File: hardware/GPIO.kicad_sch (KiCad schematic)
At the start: 21 parts, among them J10 USB_B, J8 Conn_02x10_Odd_Even, J9 Conn_01x06_Male, SW1 SW_Push, U1 MCP23008-xP, U3 PIC18F4550-IP, U4 74LS06, U5 74LS06

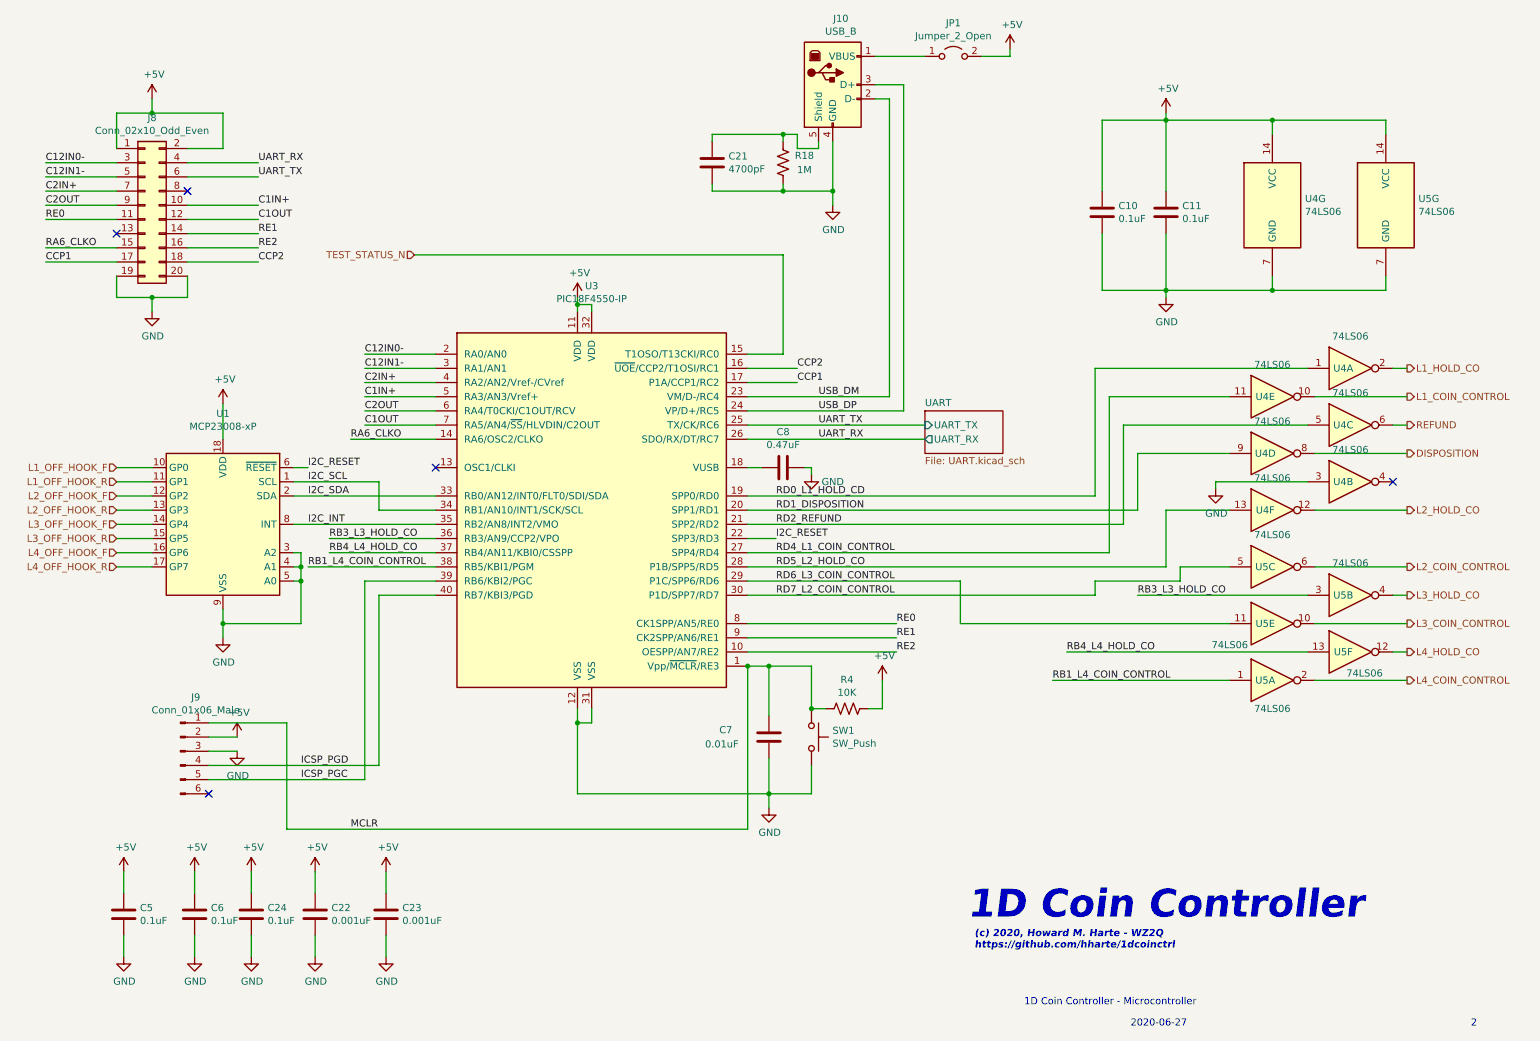
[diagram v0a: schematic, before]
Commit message: Issue 3:
* Remove barrel jack, replace with 4-position terminal block with
  provision for +/- 130VDC input in case the user already has an
  appropriate power supply and does not want the on-board
  DC-DC converter.  Note: 130V DC-DC converter PS2, relay
  K8, C14, D10, and R16 must be omitted during assembly.
* Add bi-color LEDs for line status.
  Green=Off-hook, normal polarity.
  Red=Off-hook, reverse polarity.
  Off=on-hook.
* Add header for FTDI USB UART, if user does not RS-232 UART levels.
  To use the FTDI header, do not populate U1 and other components on
  pp. 3 of the schematic.
* Remove i2c I/O expander and use PIC GPIOs directly.
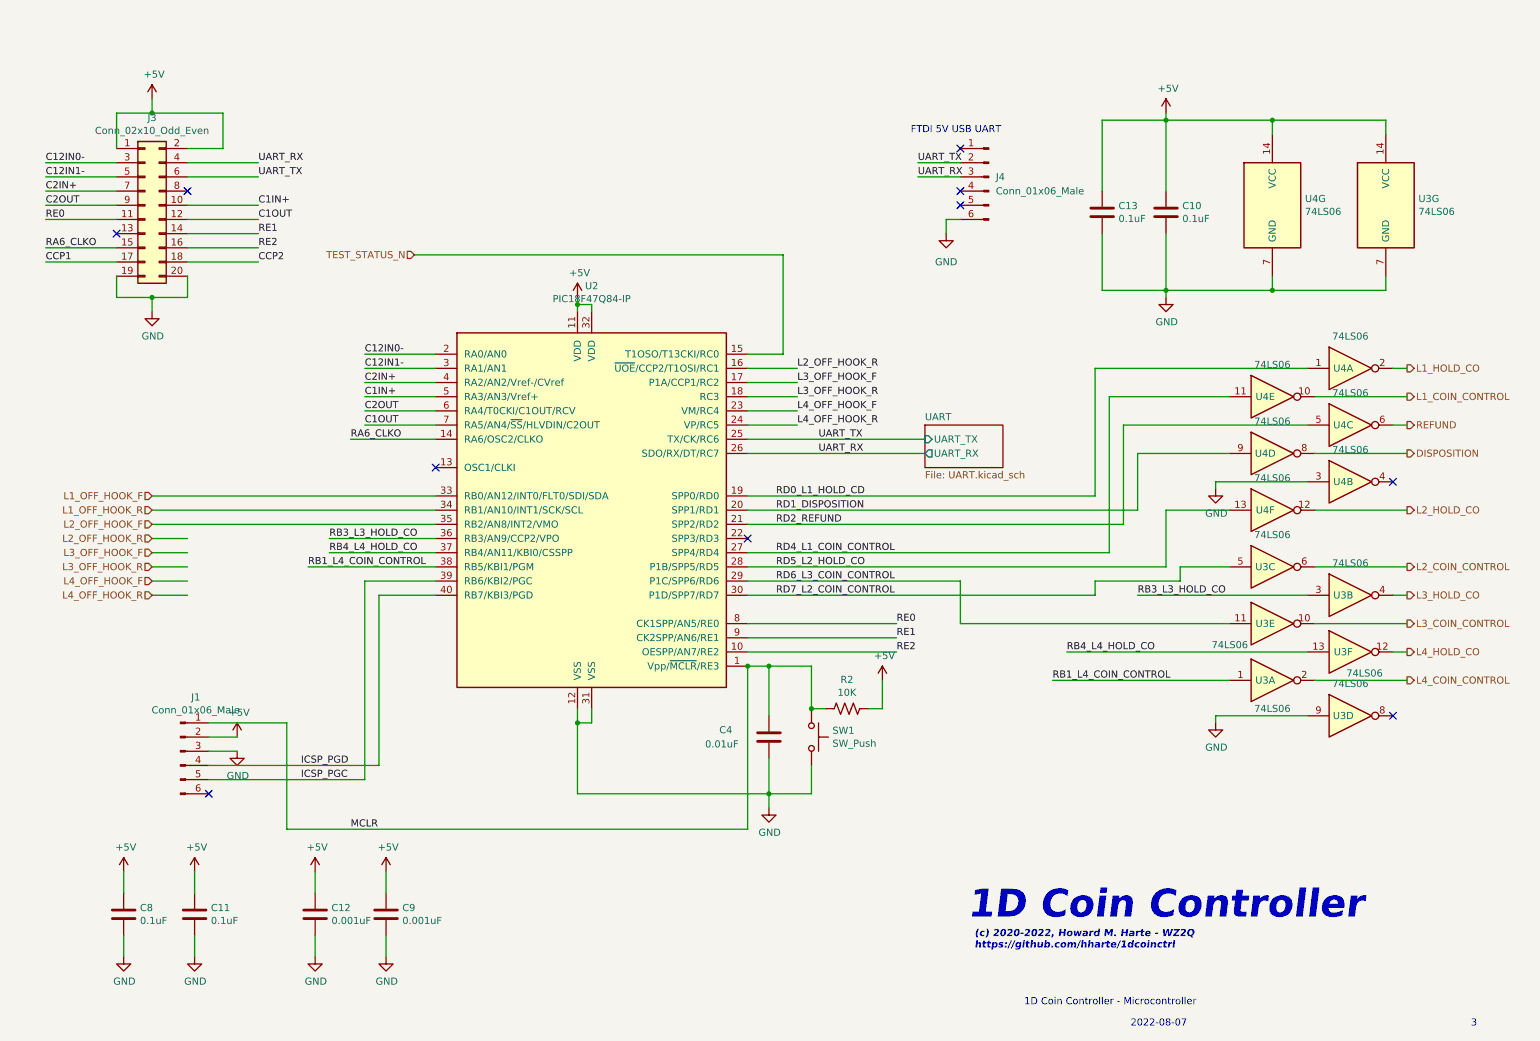
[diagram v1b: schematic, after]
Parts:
- removed C21: 4700pF, Capacitor_THT:C_Disc_D4.3mm_W1.9mm_P5.00mm, symbol Device:C
- removed C24: 0.1uF, Capacitor_THT:C_Disc_D3.0mm_W2.0mm_P2.50mm, symbol Device:C
- removed C8: 0.47uF, Capacitor_THT:C_Disc_D3.0mm_W1.6mm_P2.50mm, symbol Device:C
- removed J10: USB_B, Connector_USB:USB_B_OST_USB-B1HSxx_Horizontal, symbol Connector:USB_B
- removed JP1: Jumper_2_Open, Connector_PinHeader_2.54mm:PinHeader_1x02_P2.54mm_Vertical, symbol Jumper:Jumper_2_Open
- removed R18: 1M, Resistor_THT:R_Axial_DIN0207_L6.3mm_D2.5mm_P7.62mm_Horizontal, symbol Device:R_US
- removed U1: MCP23008-xP, Package_DIP:DIP-18_W7.62mm, symbol Interface_Expansion:MCP23008-xP
- added J4: Conn_01x06_Male, Connector_PinHeader_2.54mm:PinHeader_1x06_P2.54mm_Horizontal, symbol Connector:Conn_01x06_Male
- added unit 4 of U3
- U2: renamed from U3; value PIC18F4550-IP -> PIC18F47Q84-IP
- renumbered C11 to C10, C6 to C11, C22 to C12, C10 to C13, C7 to C4, C5 to C8, C23 to C9, J9 to J1, J8 to J3, R4 to R2, U5 to U3
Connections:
- net I2C_INT is gone; now on net L2_OFF_HOOK_F: U2.35 (RB2/AN8/INT2/VMO)
- net I2C_SCL is gone; now on net L1_OFF_HOOK_R: U2.34 (RB1/AN10/INT1/SCK/SCL)
- net I2C_SDA is gone; now on net L1_OFF_HOOK_F: U2.33 (RB0/AN12/INT0/FLT0/SDI/SDA)
- net USB_DM is gone; now on net L4_OFF_HOOK_F: U2.23 (VM/RC4)
- net USB_DP is gone; now on net L4_OFF_HOOK_R: U2.24 (VP/RC5)
- net CCP1: no longer U2.17 (P1A/CCP1/RC2)
- net CCP2: no longer U2.16 (~{UOE}/CCP2/T1OSI/RC1)
- net GND: now also J4.6 (Pin_6), U3.9
- net L2_OFF_HOOK_R: now also U2.16 (~{UOE}/CCP2/T1OSI/RC1)
- net L3_OFF_HOOK_F: now also U2.17 (P1A/CCP1/RC2)
- net L3_OFF_HOOK_R: now also U2.18 (RC3)
- net UART_RX: now also J4.3 (Pin_3)
- net UART_TX: now also J4.2 (Pin_2)
- net I2C_RESET: no longer names the net of U2.22 (SPP3/RD3)
- no-connect marks 5 -> 10
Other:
- note added: "(c) 2020-2022, Howard M. Harte - WZ2Q https://github.com/hharte/1dcoinctrl"
- note added: "2022-08-07"
- note added: "3"
- note added: "FTDI 5V USB UART"
- note removed: "(c) 2020, Howard M. Harte - WZ2Q https://github.com/hharte/1dcoinctrl"
- note removed: "2"
- note removed: "2020-06-27"

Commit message: Issue 4: Switch from PIC to AVR128DA28 MCU.
    * The AVR128DA28 is supported by the Arduino IDE.
    * Simpler UPDI programming.
    * Update to KiCAD 8.0.1
    * Fix footprint outline for IA1224S DC-DC converter.
    * Add initial Arduino firmware for AVR128DA28 MCU.
    * Move Earth Ground hole.
    * Add jumpers for UART and UPDI configuration.
    * Add 3D-printable end caps for Hammond enclosure.
    * Geographical reannotate PCB.
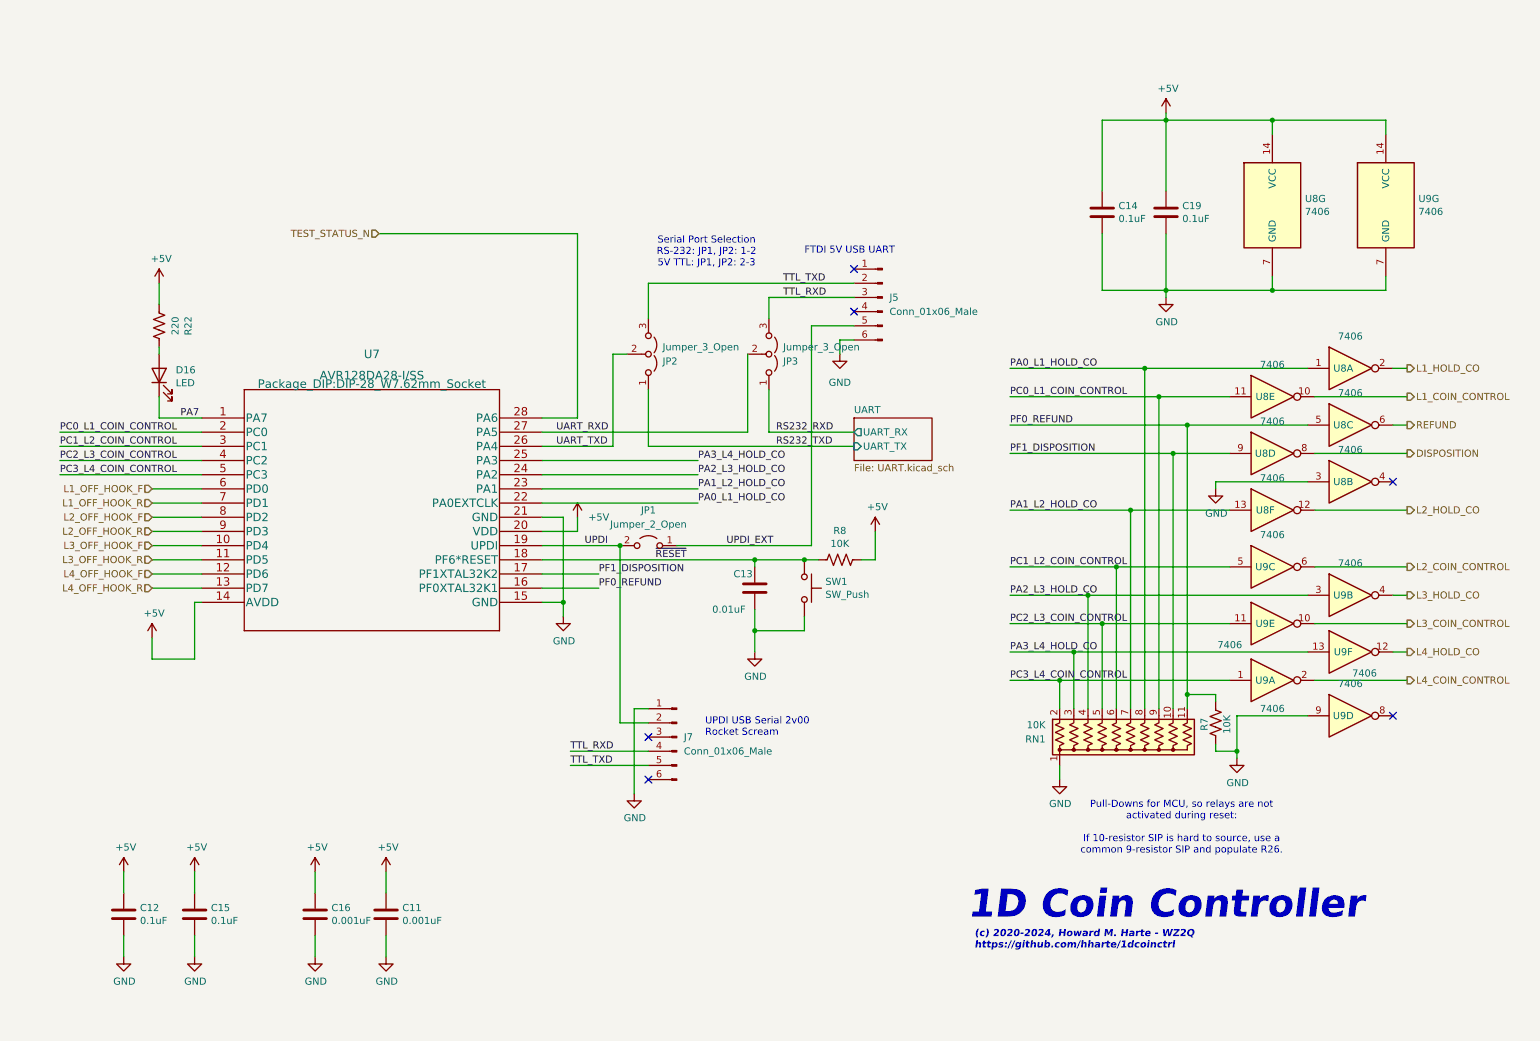
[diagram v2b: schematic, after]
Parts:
- removed C4: 0.01uF, Capacitor_THT:C_Disc_D3.0mm_W1.6mm_P2.50mm, symbol Device:C
- removed J1: Conn_01x06_Male, Connector_PinHeader_2.54mm:PinHeader_1x06_P2.54mm_Vertical, symbol Connector:Conn_01x06_Male
- removed J3: Conn_02x10_Odd_Even, Connector_IDC:IDC-Header_2x10_P2.54mm_Vertical, symbol Connector_Generic:Conn_02x10_Odd_Even
- removed U2: PIC18F47Q84-IP, Package_DIP:DIP-40_W15.24mm, symbol MCU_Microchip_PIC18:PIC18F4550-IP
- added C13: 0.01uF, Capacitor_THT:C_Disc_D3.0mm_W1.6mm_P2.50mm, symbol Device:C
- added D16: LED, LED_THT:LED_D5.0mm, symbol Device:LED
- added J7: Conn_01x06_Male, Connector_PinHeader_2.54mm:PinHeader_1x06_P2.54mm_Vertical, symbol Connector:Conn_01x06_Male
- added JP1: Jumper_2_Open, Connector_PinHeader_2.54mm:PinHeader_1x02_P2.54mm_Vertical, symbol Jumper:Jumper_2_Open
- added JP2, JP3: Jumper_3_Open, Connector_PinHeader_2.54mm:PinHeader_1x03_P2.54mm_Vertical, symbol Jumper:Jumper_3_Open
- added R22: 220, Resistor_THT:R_Axial_DIN0207_L6.3mm_D2.5mm_P7.62mm_Horizontal, symbol Device:R_US
- added R7: 10K, Resistor_THT:R_Axial_DIN0207_L6.3mm_D2.5mm_P7.62mm_Horizontal, symbol Device:R_US
- added RN1: 10K, Resistor_THT:R_Array_SIP11, symbol Device:R_Network10_US
- added U7: AVR128DA28-I/SS, Package_DIP:DIP-28_W7.62mm_Socket, symbol AVR128DA28:AVR128DA28-I{brace}slash}SS
- C11: renamed from C9; Digi-Key_PN (none) -> 56-K102M15X7RF5UL2CT-ND; MPN (none) -> K102M15X7RF5UL2
- C12: renamed from C8; Digi-Key_PN (none) -> 56-K104M15X7RF5TL2CT-ND; MPN (none) -> K104M15X7RF5TL2
- C14: renamed from C13; Digi-Key_PN (none) -> 56-K104M15X7RF5TL2CT-ND; MPN (none) -> K104M15X7RF5TL2
- C15: renamed from C11; Digi-Key_PN (none) -> 56-K104M15X7RF5TL2CT-ND; MPN (none) -> K104M15X7RF5TL2
- C16: renamed from C12; Digi-Key_PN (none) -> 56-K102M15X7RF5UL2CT-ND; MPN (none) -> K102M15X7RF5UL2
- C19: renamed from C10; Digi-Key_PN (none) -> 56-K104M15X7RF5TL2CT-ND; MPN (none) -> K104M15X7RF5TL2
- J5: renamed from J4; Digi-Key_PN (none) -> 732-5339-ND; MPN (none) -> 61300611021
- R8: renamed from R2; Digi-Key_PN (none) -> S10KHCT-ND; MPN (none) -> CFM12JT10K0
- SW1: Digi-Key_PN (none) -> 486-3458-ND; MPN (none) -> 1301.9302
- U8: renamed from U4; value 74LS06 -> 7406; Digi-Key_PN (none) -> 296-1435-5-ND; MPN (none) -> SN7406N
- U9: renamed from U3; value 74LS06 -> 7406; Digi-Key_PN (none) -> 296-1435-5-ND; MPN (none) -> SN7406N
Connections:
- net +5V: now also R22.2, U7.14 (AVDD), U7.20 (VDD)
- net GND: now also C13.2, J7.1 (Pin_1), R7.2, RN1.1 (common), U7.15 (GND), U7.21 (GND)
- net L1_OFF_HOOK_F: now also U7.6 (PD0)
- net L1_OFF_HOOK_R: now also U7.7 (PD1)
- net L2_OFF_HOOK_F: now also U7.8 (PD2)
- net L2_OFF_HOOK_R: now also U7.9 (PD3)
- net L3_OFF_HOOK_F: now also U7.10 (PD4)
- net L3_OFF_HOOK_R: now also U7.11 (PD5)
- net L4_OFF_HOOK_F: now also U7.12 (PD6)
- net L4_OFF_HOOK_R: now also U7.13 (PD7)
- net TEST_STATUS_N: now also U7.28 (PA6)
- net UPDI_EXT: now reaches J5.5 (Pin_5)
- net UPDI_EXT: now also JP1.1 (A)
- net MCLR renamed ~{RESET}
- net ~{RESET}: now also C13.1, U7.18 (PF6*RESET)
- net RB1_L4_COIN_CONTROL renamed PC3_L4_COIN_CONTROL
- net PC3_L4_COIN_CONTROL: now also RN1.2 (R1), U7.5 (PC3)
- net RB3_L3_HOLD_CO renamed PA2_L3_HOLD_CO
- net PA2_L3_HOLD_CO: now also RN1.4 (R3), U7.24 (PA2)
- net RB4_L4_HOLD_CO renamed PA3_L4_HOLD_CO
- net PA3_L4_HOLD_CO: now also RN1.3 (R2), U7.25 (PA3)
- net RD0_L1_HOLD_CD renamed PA0_L1_HOLD_CO
- net PA0_L1_HOLD_CO: now also RN1.8 (R7), U7.22 (PA0EXTCLK)
- net RD1_DISPOSITION renamed PF1_DISPOSITION
- net PF1_DISPOSITION: now also RN1.10 (R9), U7.17 (PF1XTAL32K2)
- net RD2_REFUND renamed PF0_REFUND
- net PF0_REFUND: now also R7.1, RN1.11 (R10), U7.16 (PF0XTAL32K1)
- net RD4_L1_COIN_CONTROL renamed PC0_L1_COIN_CONTROL
- net PC0_L1_COIN_CONTROL: now also RN1.9 (R8), U7.2 (PC0)
- net RD5_L2_HOLD_CO renamed PA1_L2_HOLD_CO
- net PA1_L2_HOLD_CO: now also RN1.7 (R6), U7.23 (PA1)
- net RD6_L3_COIN_CONTROL renamed PC2_L3_COIN_CONTROL
- net PC2_L3_COIN_CONTROL: now also RN1.5 (R4), U7.4 (PC2)
- net RD7_L2_COIN_CONTROL renamed PC1_L2_COIN_CONTROL
- net PC1_L2_COIN_CONTROL: now also RN1.6 (R5), U7.3 (PC1)
- net UART_RX renamed TTL_RXD
- net TTL_RXD: now also J7.4 (Pin_4), JP3.3 (B)
- net UART_TX renamed TTL_TXD
- net TTL_TXD: now also J7.5 (Pin_5), JP2.3 (B)
- new net: D16.2 (A), R22.1
- new net PA7: D16.1 (K), U7.1 (PA7)
- new net RS232_RXD: JP3.1 (A)
- new net RS232_TXD: JP2.1 (A)
- new net UART_RXD: JP3.2 (C), U7.27 (PA5)
- new net UART_TXD: JP2.2 (C), U7.26 (PA4)
- new net UPDI: J7.2 (Pin_2), JP1.2 (B), U7.19 (UPDI)
- no-connect marks 10 -> 6
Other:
- note added: "(c) 2020-2024, Howard M. Harte - WZ2Q https://github.com/hharte/1dcoinctrl"
- note added: "Pull-Downs for MCU, so relays are not activated during reset: If 10-resistor SIP is hard to source, use a common 9-resistor SIP and populate R26."
- note added: "Serial Port Selection RS-232: JP1, JP2: 1-2 5V TTL: JP1, JP2: 2-3"
- note added: "UPDI USB Serial 2v00 Rocket Scream"
- note removed: "(c) 2020-2022, Howard M. Harte - WZ2Q https://github.com/hharte/1dcoinctrl"
- note removed: "1D Coin Controller - Microcontroller"
- note removed: "2022-08-07"
- note removed: "3"
- title: (none) -> 1D Coin Controller - Microcontroller
- moved on the sheet: J5, R8, SW1
